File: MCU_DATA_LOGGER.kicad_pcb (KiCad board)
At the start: 2 copper layers, 29 parts, among them J1 Conn_01x04_Male, J2 Conn_01x04_Male, J3 Conn_01x09_Male, J4 Conn_02x03_Odd_Even, U1 DS1337S+, U2 24LC1025, U3 24LC1025, U4 ATMEGA328P-AU, Y1 32.768 KHz, Y2 16 MHz

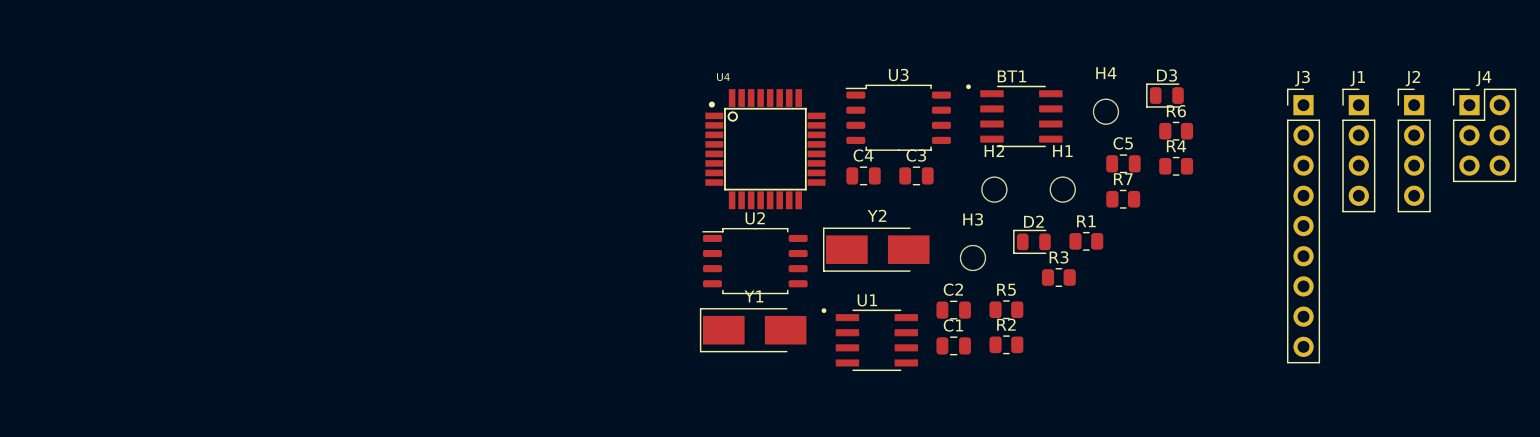
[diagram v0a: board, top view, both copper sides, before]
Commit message: Completed placement of footprints
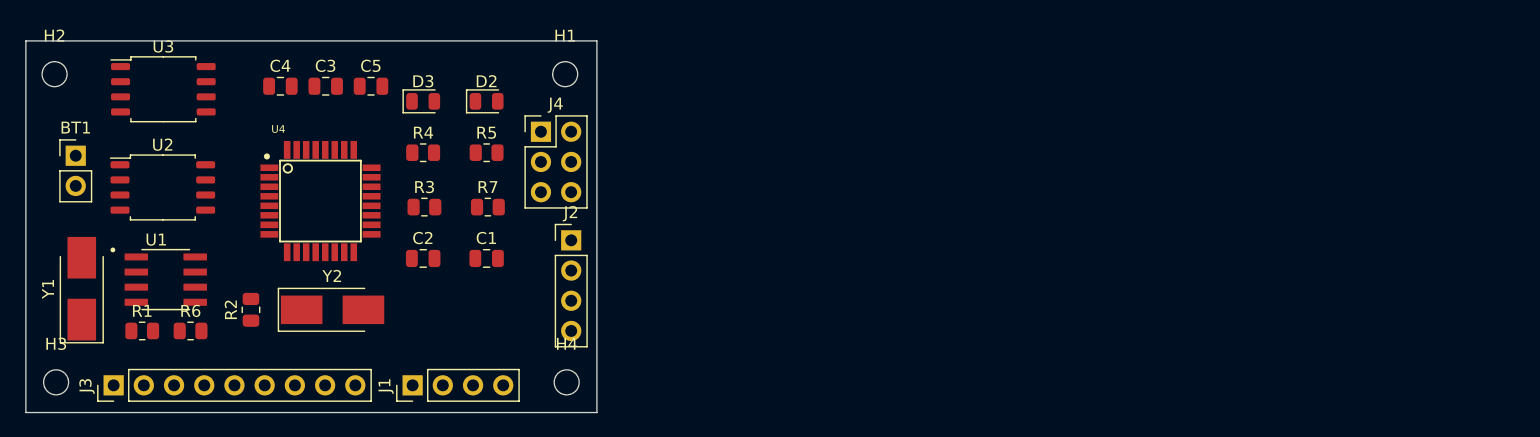
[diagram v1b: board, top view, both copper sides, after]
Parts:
- BT1: footprint DS1337S_:SOIC127P600X175-8N -> Connector_PinHeader_2.54mm:PinHeader_1x02_P2.54mm_Vertical
- moved J3 102.8 mm to (54.5, 98.6), turned to 90 degrees
- moved R6 84.5 mm to (61.0, 94.0)
- moved J1 83.0 mm to (79.6, 98.6), turned to 90 degrees
- moved R1 79.7 mm to (56.9, 94.0)
- moved H2 79.6 mm to (49.5, 72.4)
- moved BT1 79.6 mm to (51.3, 79.2)
- moved J4 78.1 mm to (90.4, 77.2)
- moved H3 77.8 mm to (49.7, 98.3)
- moved J2 71.8 mm to (93.0, 86.4)
- moved C5 63.6 mm to (76.1, 73.4)
- moved R2 63.6 mm to (66.0, 92.2), turned to 90 degrees
- moved R4 63.3 mm to (80.5, 79.0)
- moved D3 62.5 mm to (80.5, 74.7)
- moved U3 61.9 mm to (58.7, 73.7)
- moved U1 60.0 mm to (58.9, 89.7)
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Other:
- board outline added: 48 x 31.2 mm

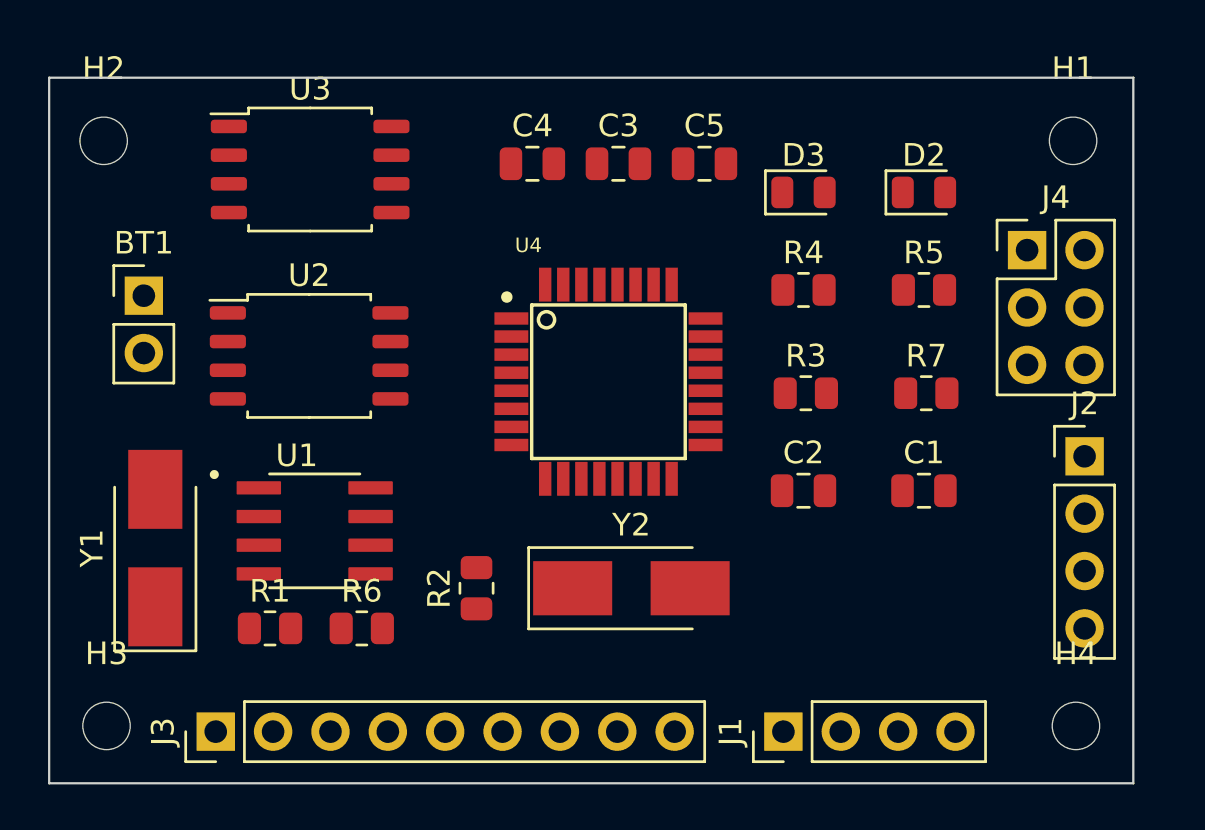
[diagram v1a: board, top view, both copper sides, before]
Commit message: Routing GND Vcc completed
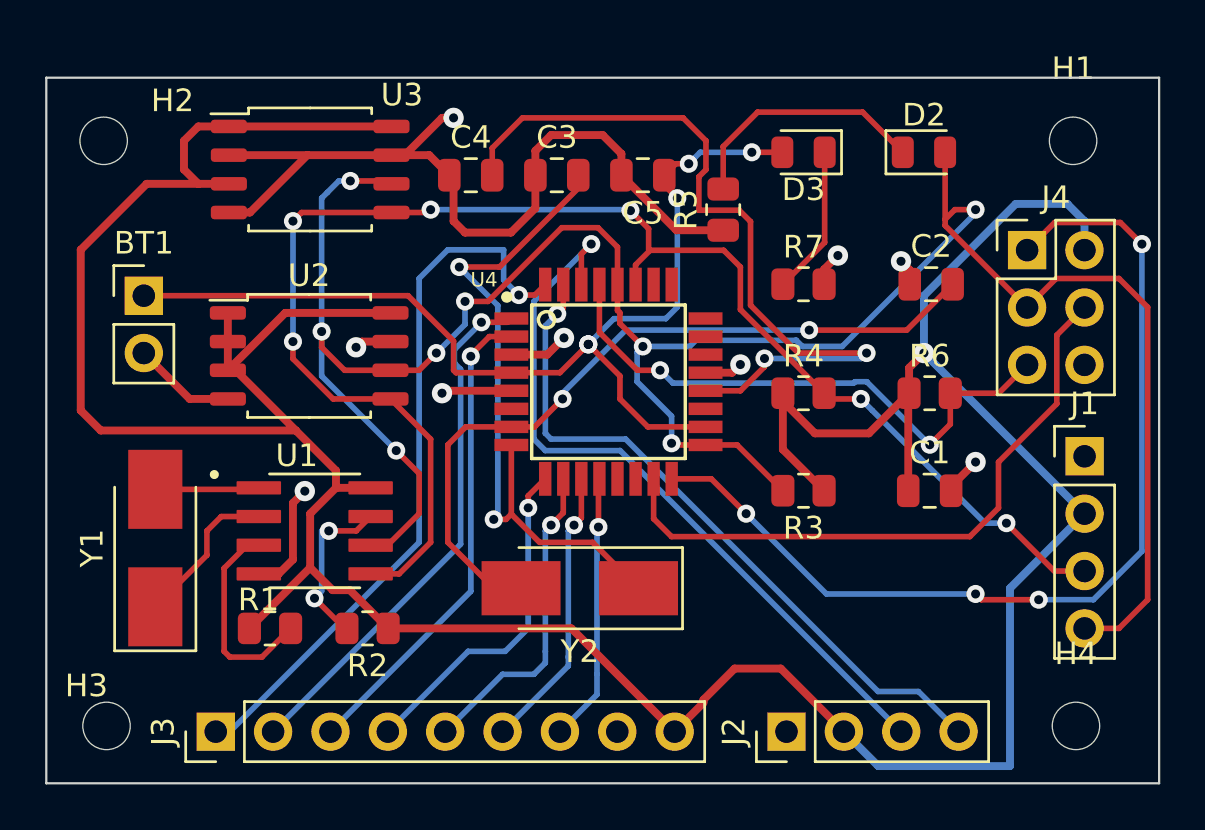
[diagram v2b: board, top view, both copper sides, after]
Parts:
- moved R6 27.2 mm to (86.1, 83.6)
- moved J1 18.1 mm to (93.0, 86.4), turned to 0 degrees
- moved J2 18.0 mm to (79.8, 98.6), turned to 90 degrees
- moved C2 10.8 mm to (86.2, 78.7)
- moved R5 9.57 mm to (77.0, 75.4), turned to 90 degrees
- moved R7 7.27 mm to (80.5, 78.7)
- moved R2 5.14 mm to (61.2, 94.0), turned to 180 degrees
- moved R4 4.57 mm to (80.5, 83.6)
- moved R3 4.32 mm to (80.5, 87.9), turned to 180 degrees
- moved C3 2.77 mm to (69.6, 73.9)
- moved C4 2.77 mm to (65.8, 73.9)
- moved C5 2.77 mm to (73.4, 73.9), turned to 180 degrees
- moved Y2 2.29 mm to (70.6, 92.2), turned to 180 degrees
- moved D2 1.78 mm to (85.9, 72.9)
- moved D3 1.78 mm to (80.5, 72.9), turned to 180 degrees
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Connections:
- J2 pad 3: /Tx -> /Rx
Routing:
- net /Vcc: track 0.00 -> 155.4 mm, vias 0 -> 1
- net /SCK: track 0.00 -> 105.6 mm, vias 0 -> 8
- net /SDA: track 0.00 -> 66.8 mm, vias 0 -> 6
- net GND: track 0.00 -> 61.3 mm, vias 0 -> 9
- net Net-(BT1-Pad1): track 0.00 -> 46.0 mm, vias 0 -> 5
- net /MISO: track 0.00 -> 43.5 mm, vias 0 -> 4
- net Net-(C4-Pad2): track 0.00 -> 35.1 mm, vias 0 -> 2
- net Net-(C2-Pad2): track 0.00 -> 33.8 mm, vias 0 -> 2
- net /Rx: track 0.00 -> 33.3 mm, vias 0 -> 1
- net /D2: track 0.00 -> 32.1 mm, vias 0 -> 1
- net /Tx: track 0.00 -> 30.7 mm, vias 0 -> 1
- net Net-(C3-Pad2): track 0.00 -> 30.2 mm, vias 0 -> 2
- net /MOSI: track 0.00 -> 28.3 mm
- net /RESET: track 0.00 -> 25.4 mm, vias 0 -> 2
- net /D3: track 0.00 -> 23.6 mm, vias 0 -> 1
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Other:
- board size 48 x 31.2 mm -> 49.3 x 31.2 mm

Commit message: Completed routing and Zones
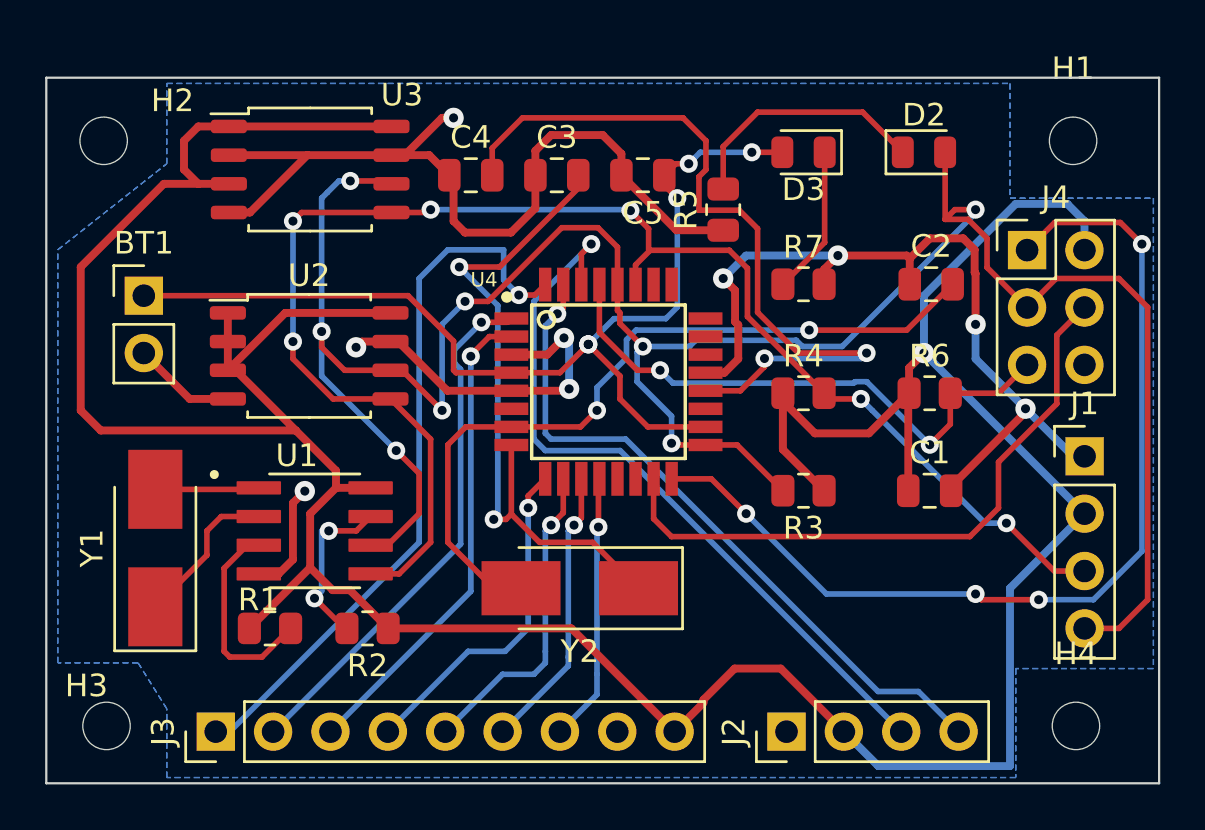
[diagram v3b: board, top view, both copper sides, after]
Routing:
- net GND: track 61.3 -> 100.2 mm
- net /SCK: track 105.6 -> 109.3 mm
- net Net-(C2-Pad2): track 33.8 -> 34.8 mm
- added copper zone on B.Cu, net GND

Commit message: fixed all issues
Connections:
- BT1 pad 1: Net-(BT1-Pad1) -> /Vcc
- C5 pad 1: Net-(BT1-Pad1) -> /Vcc
- D3 pad 2: Net-(BT1-Pad1) -> /Vcc
- U4 pad 18: Net-(BT1-Pad1) -> /Vcc
- U4 pad 4: Net-(BT1-Pad1) -> /Vcc
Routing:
- net /Vcc: track 154.9 -> 203.0 mm, vias 1 -> 6
- net Net-(BT1-Pad1): track 46.0 -> 0.00 mm, vias 5 -> 0
